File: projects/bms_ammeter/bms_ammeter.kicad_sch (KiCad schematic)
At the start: 6 parts, among them IC1 ADS1246IPWR, U1 AP7370-33Y-13

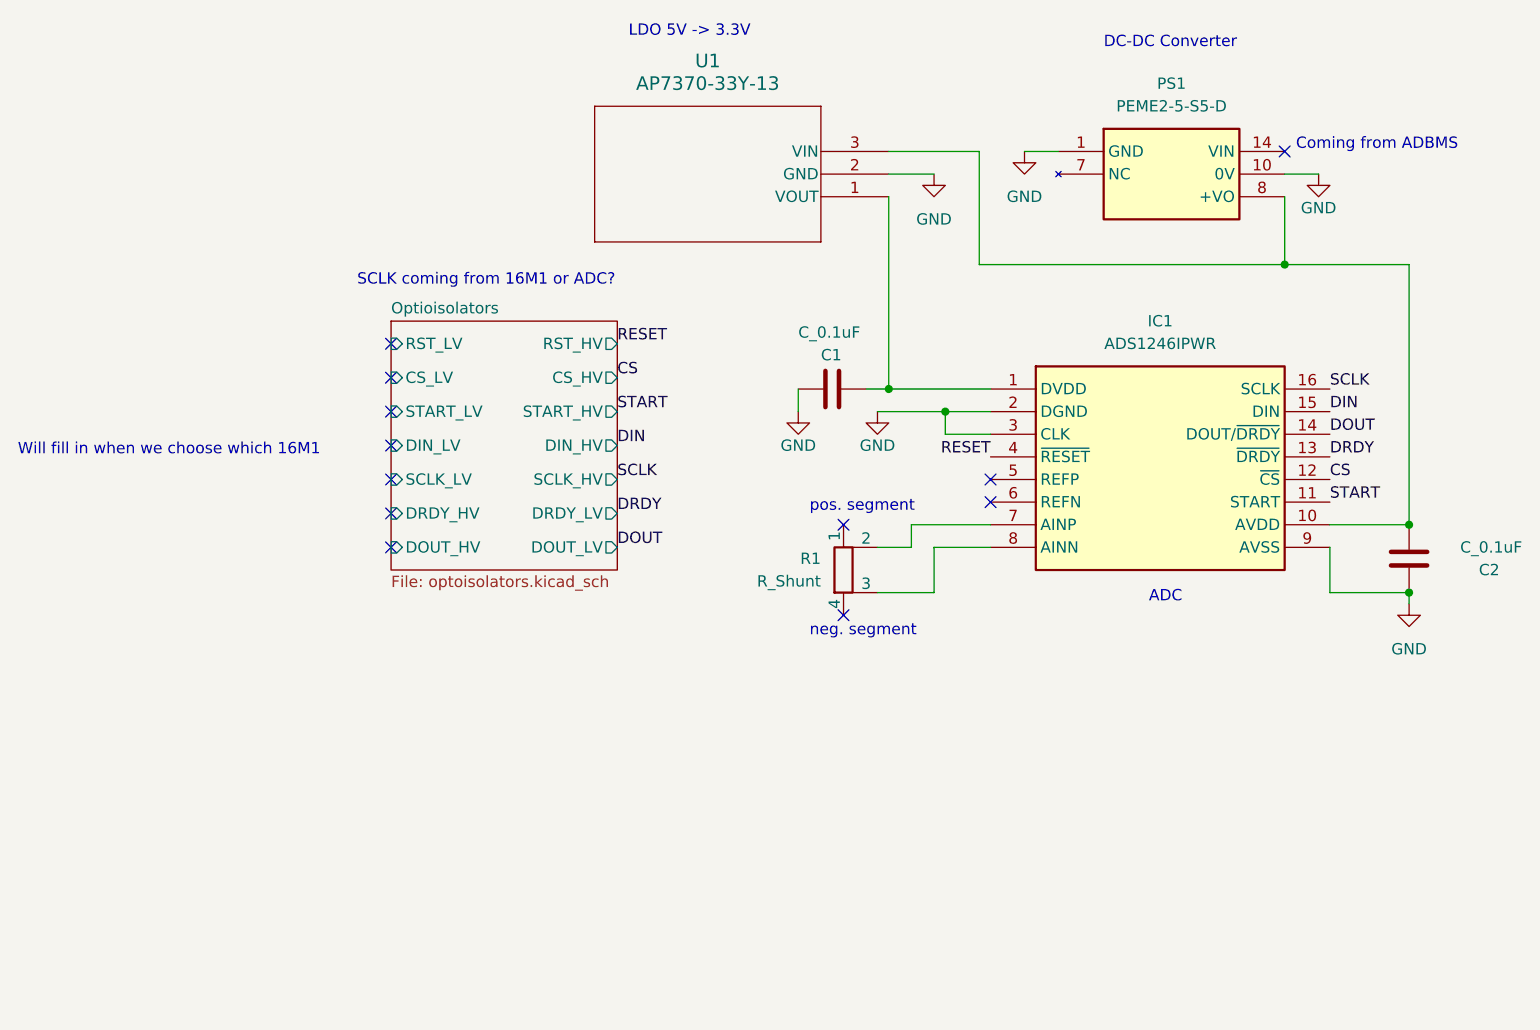
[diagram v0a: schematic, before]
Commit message: add spisolator
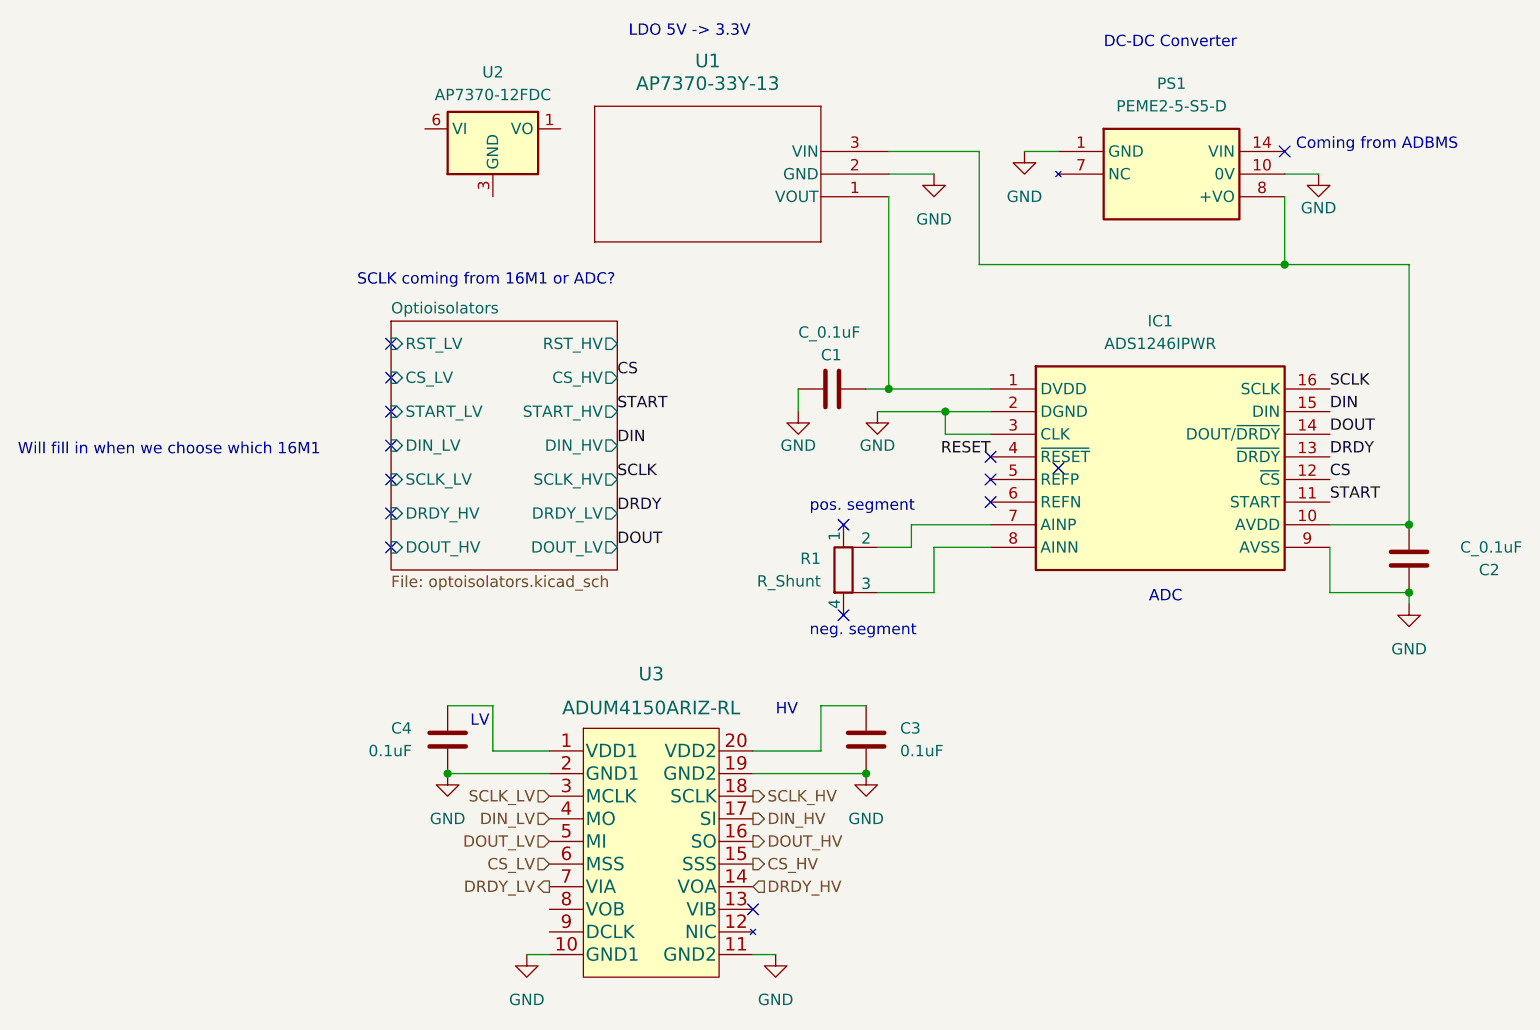
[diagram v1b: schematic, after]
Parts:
- added C3, C4: 0.1uF, Capacitor_SMD:C_0201_0603Metric, symbol Device:C
- added U2: AP7370-12FDC, Package_DFN_QFN:DFN-6-1EP_2x2mm_P0.65mm_EP1.01x1.7mm, symbol Regulator_Linear:AP7370-12FDC
- added U3: ADUM4150ARIZ-RL, footprints:20-SOIC, symbol formula:ADUM4150ARIZ-RL
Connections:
- net GND: now also C3.2, C4.2, U3.10 (GND1), U3.11 (GND2), U3.19 (GND2), U3.2 (GND1)
- new net: C4.1, U3.1 (VDD1)
- new net: C3.1, U3.20 (VDD2)
- new net: U2.3 (GND), U2.7 (GND)
- new net CS_HV: U3.15 (SSS)
- new net CS_LV: U3.6 (MSS)
- new net DIN_HV: U3.17 (SI)
- new net DIN_LV: U3.4 (MO)
- new net DOUT_HV: U3.16 (SO)
- new net DOUT_LV: U3.5 (MI)
- new net DRDY_HV: U3.14 (VOA)
- new net DRDY_LV: U3.7 (VIA)
- new net SCLK_HV: U3.18 (SCLK)
- new net SCLK_LV: U3.3 (MCLK)
- no-connect marks 12 -> 15
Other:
- note added: "HV"
- note added: "LV"
